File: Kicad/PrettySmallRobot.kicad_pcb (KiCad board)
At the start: 4 copper layers, 25.6 x 25 mm, 56 parts, among them J1 TYPE-C-31-M-12, J2 MOTORA_1, J3 MOTORA_2, J4 MOTORB_1, J5 MOTORB_2, J6 BATT+, J7 GND, U1 DRV8837, U2 DRV8837, U3 MCP73831-2ACI_MC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

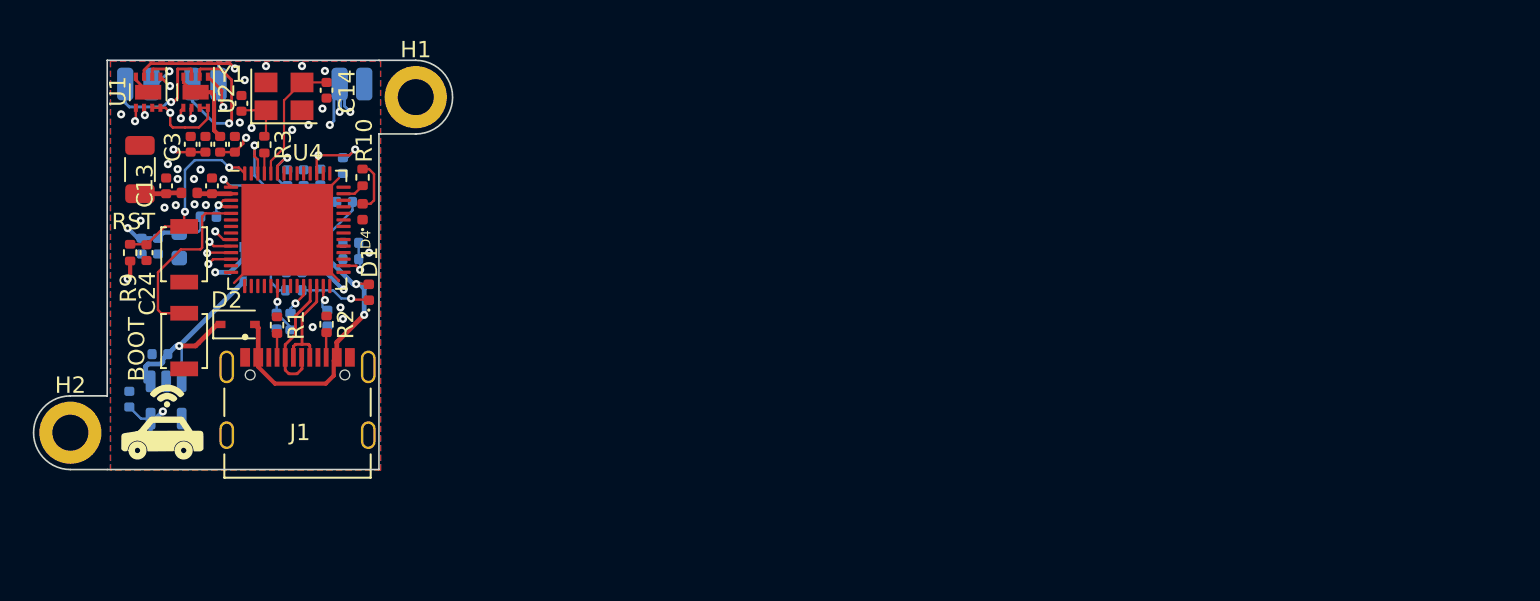
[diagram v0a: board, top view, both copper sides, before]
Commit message: ripped up all routing to start again to fit the new cad
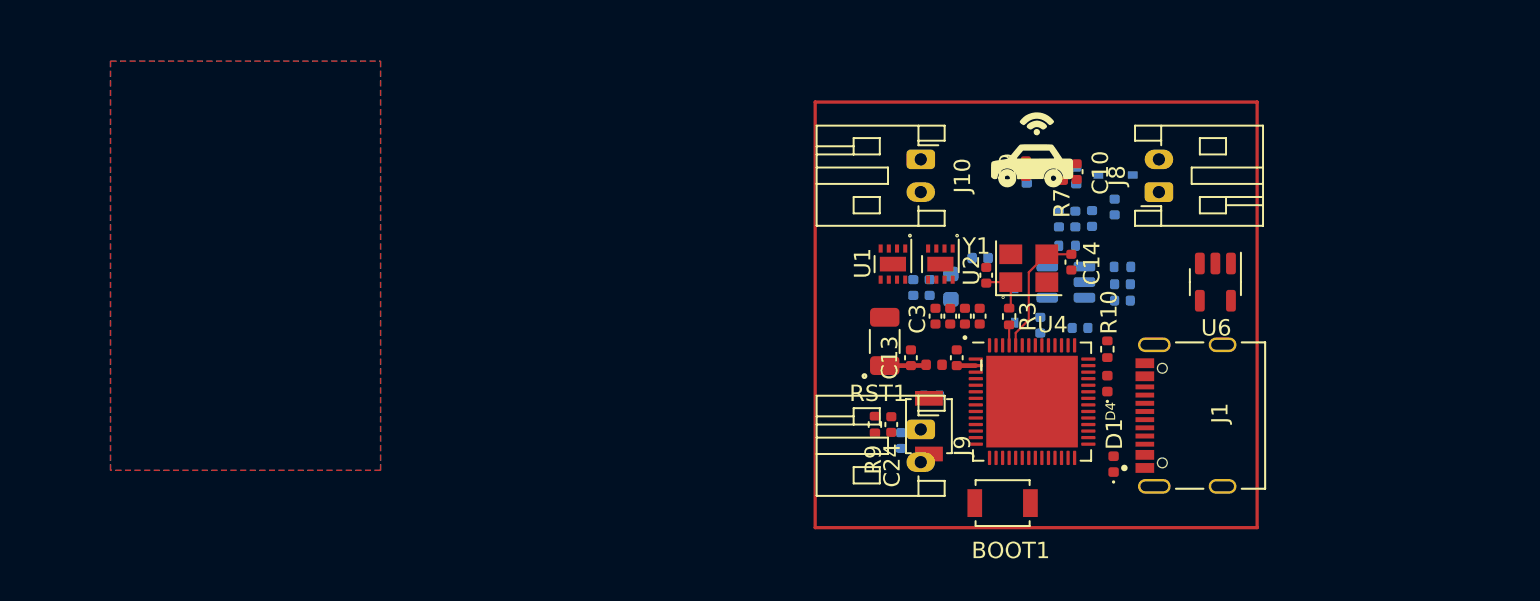
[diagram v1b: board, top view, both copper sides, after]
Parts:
- removed H1, H2: MountingHole, MountingHole:MountingHole_2.2mm_M2_DIN965_Pad
- removed J2: MOTORA_1, Connector_Wire:SolderWirePad_1x01_SMD_1x2mm
- removed J3: MOTORA_2, Connector_Wire:SolderWirePad_1x01_SMD_1x2mm
- removed J4: MOTORB_1, Connector_Wire:SolderWirePad_1x01_SMD_1x2mm
- removed J5: MOTORB_2, Connector_Wire:SolderWirePad_1x01_SMD_1x2mm
- removed J6: BATT+, Connector_Wire:SolderWirePad_1x01_SMD_1x2mm
- removed J7: GND, Connector_Wire:SolderWirePad_1x01_SMD_1x2mm
- added J10: Conn_01x02, Connector_JST:JST_PH_S2B-PH-K_1x02_P2.00mm_Horizontal, F.Cu at (177.0, 102.5)
- added J8: Conn_01x02, Connector_JST:JST_PH_S2B-PH-K_1x02_P2.00mm_Horizontal, F.Cu at (191.6, 104.5)
- added J9: Conn_01x02, Connector_JST:JST_PH_S2B-PH-K_1x02_P2.00mm_Horizontal, F.Cu at (177.0, 119.0)
- C10, C9, R7, U6: moved to F.Cu
- D2, R1, R2: moved to B.Cu
- U3: value MCP73831-2ACI_MC -> MCP73831-2-OT; footprint kicad_footprints:SON50P200X300X100-9N -> Package_TO_SOT_SMD:SOT-23-5
- moved U6 64.5 mm to (195.0, 110.0)
- moved J1 56.5 mm to (195.4, 118.2), turned to 90 degrees
- moved D2 54.4 mm to (188.9, 103.5), turned to 180 degrees
- moved BOOT1 51.0 mm to (182.0, 123.5), turned to 0 degrees
- moved R5 50.6 mm to (189.3, 109.1)
- moved C10 49.7 mm to (186.5, 103.3)
- moved R1 49.7 mm to (186.5, 103.5)
- moved R7 48.0 mm to (185.7, 103.3)
- moved C1 47.2 mm to (178.8, 110.3)
- moved C19 47.2 mm to (187.5, 106.1)
- moved C8 47.2 mm to (188.8, 105.4)
- moved D3 47.2 mm to (182.7, 111.4)
- moved C11 47.2 mm to (189.3, 111.1)
- moved C16 47.2 mm to (189.3, 110.1)
- moved C18 47.2 mm to (186.4, 106.2)
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- renumbered BOOT to BOOT1, RST to RST1
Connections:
- U3 pad 1: /VBUS -> Net-(R5-Pad2)
- U3 pad 2: /VBUS -> GND
- U3 pad 4: +BATT -> /VBUS
- U3 pad 5: Net-(R5-Pad2) -> Net-(R6-Pad2)
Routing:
- net +BATT: track 64.8 -> 0.00 mm, vias 8 -> 0
- net +3V3: track 35.6 -> 0.00 mm, vias 11 -> 0
- net /VBUS: track 22.9 -> 0.00 mm, vias 2 -> 0
- net GND: track 22.1 -> 0.00 mm, vias 24 -> 0
- net /VDDA: track 16.2 -> 0.00 mm, vias 3 -> 0
- net /MOTORB_IN2: track 16.0 -> 0.00 mm, vias 2 -> 0
- net /MOTORA_IN2: track 15.9 -> 0.00 mm, vias 2 -> 0
- net Net-(C22-Pad1): track 14.5 -> 0.00 mm, vias 1 -> 0
- net /MOTORA_IN1: track 14.2 -> 0.00 mm, vias 2 -> 0
- net /MOTORB_IN1: track 13.5 -> 0.00 mm, vias 2 -> 0
- net /~{RESET}: track 11.5 -> 0.00 mm, vias 2 -> 0
- net /BOOT: track 11.0 -> 0.00 mm
- net /MOTORB_OUT1: track 9.24 -> 0.00 mm, vias 1 -> 0
- net /MOTORA_OUT2: track 8.61 -> 0.00 mm, vias 1 -> 0
- net /MOTORB_OUT2: track 7.75 -> 0.00 mm, vias 1 -> 0
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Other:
- board outline removed
- board text added: "Mounting Clip"

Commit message: resized board to 29x27mm
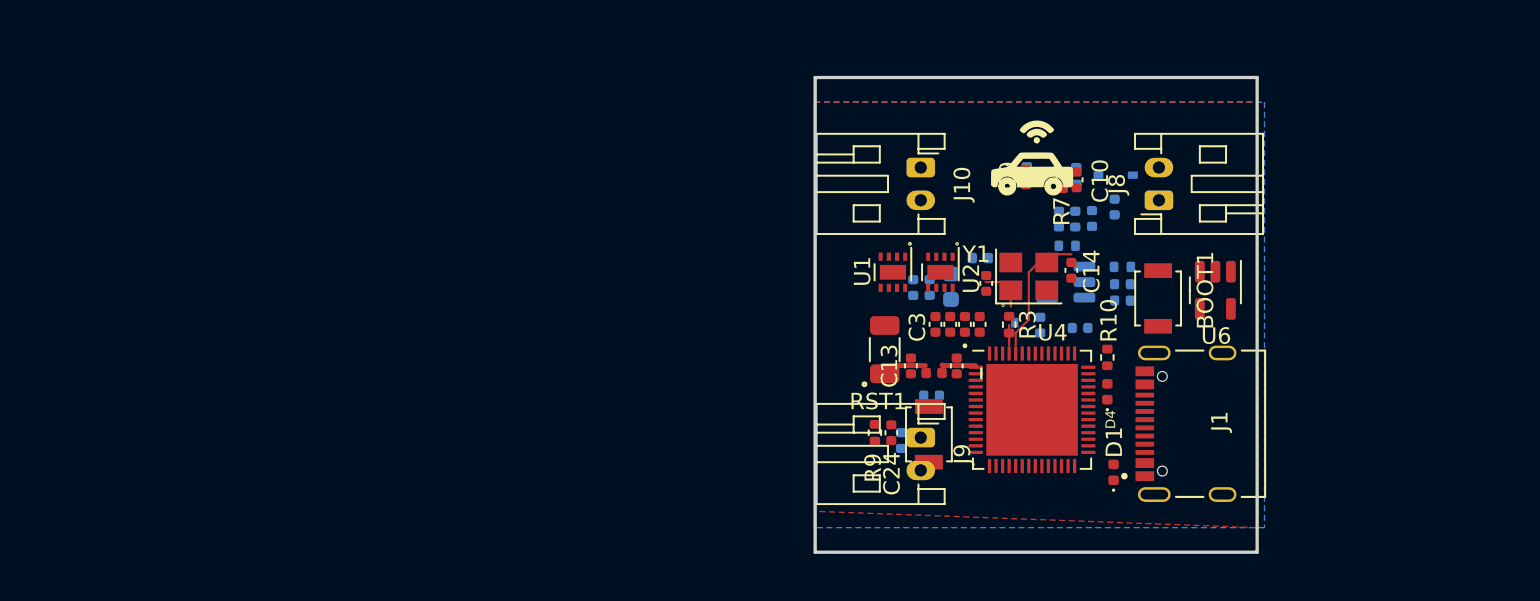
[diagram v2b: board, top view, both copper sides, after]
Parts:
- moved BOOT1 15.7 mm to (191.5, 111.0), turned to 90 degrees
- moved AE1 0.50 mm to (174.8, 114.1)
- moved C10 0.50 mm to (186.5, 103.8)
- moved C13 0.50 mm to (176.4, 115.1)
- moved C14 0.50 mm to (186.2, 109.3)
- moved C15 0.50 mm to (181.0, 110.1)
- moved C17 0.50 mm to (179.2, 115.1)
- moved C2 0.50 mm to (180.6, 112.6)
- moved C24 0.50 mm to (175.2, 119.2)
- moved C3 0.50 mm to (177.9, 112.6)
- moved C6 0.50 mm to (178.8, 112.6)
- moved C7 0.50 mm to (179.7, 112.6)
- moved C9 0.50 mm to (183.4, 103.6)
- moved D1 0.50 mm to (188.8, 121.6)
- moved D4 0.50 mm to (188.4, 116.7)
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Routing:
- net Net-(C17-Pad1): track 1.16 -> 2.08 mm
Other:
- board outline added: 27 x 29 mm

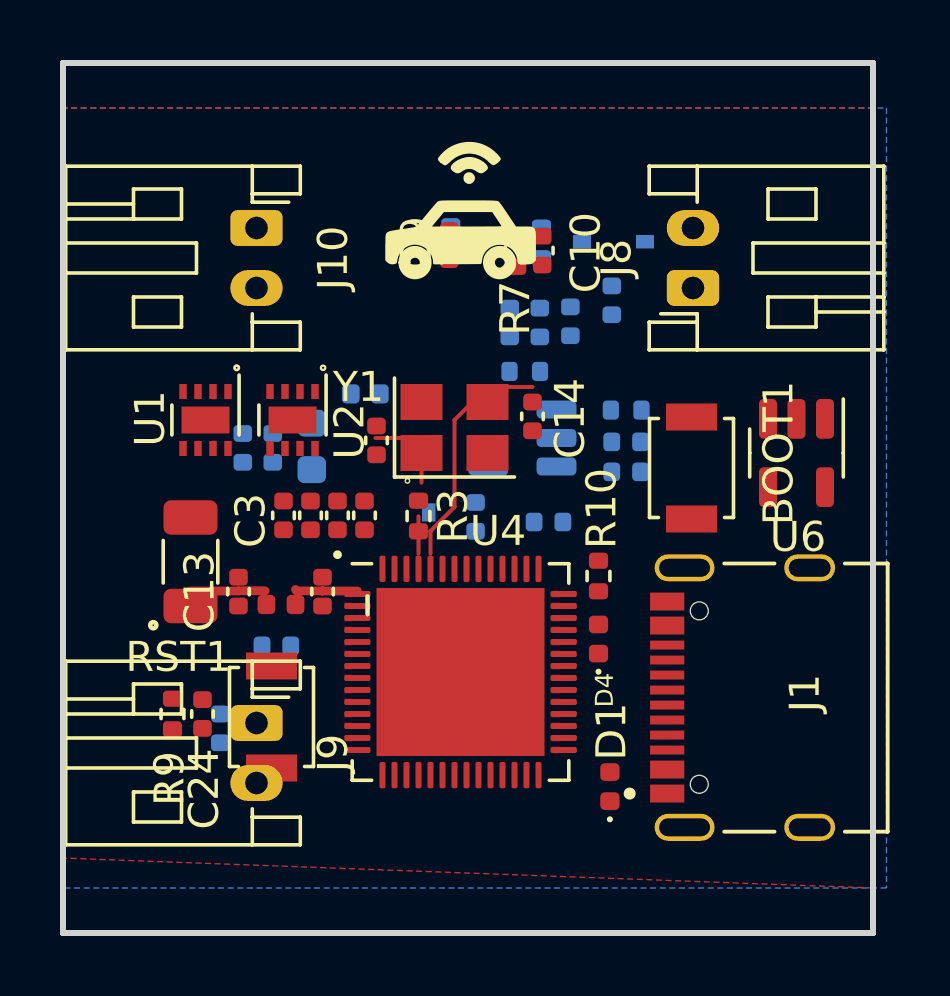
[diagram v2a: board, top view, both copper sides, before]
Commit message: resized board again to 29x26mm
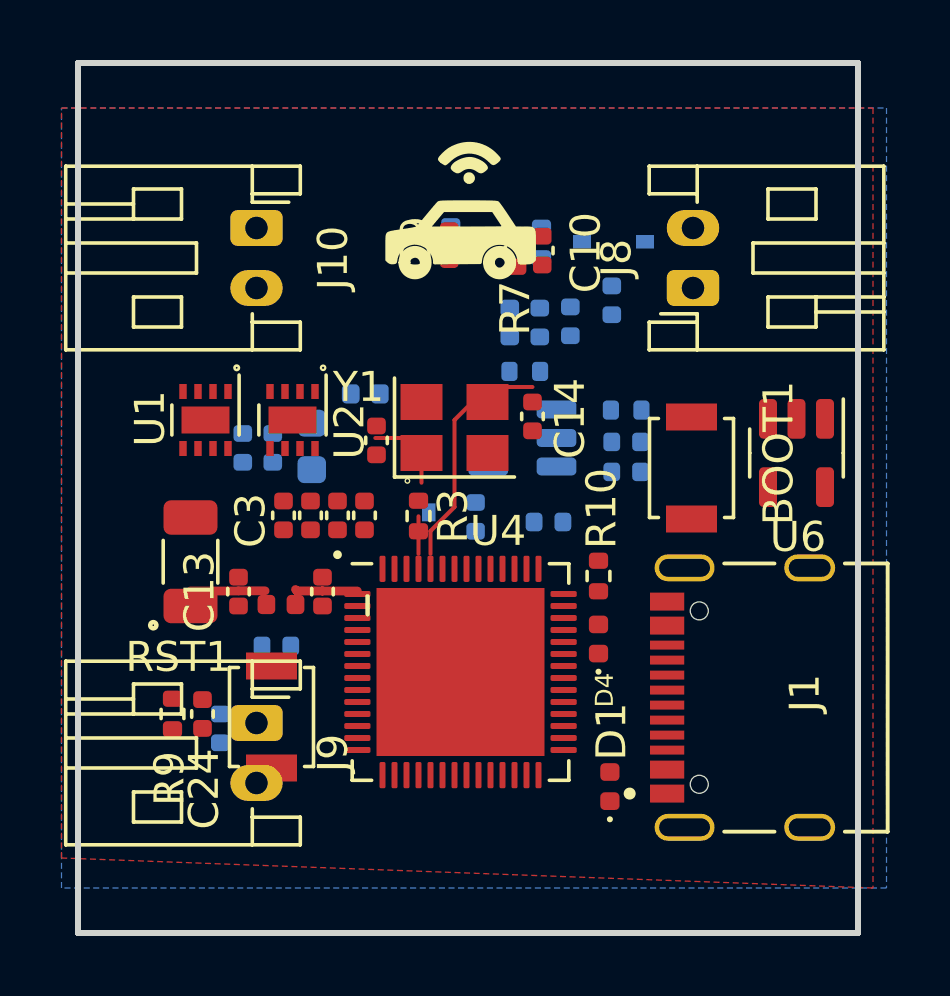
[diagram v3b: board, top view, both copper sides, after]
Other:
- board size 27 x 29 mm -> 26 x 29 mm
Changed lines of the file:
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@@
       (xy 184.129503 100.179194)
     ) (layer "F.SilkS") (width 0.1) (fill solid))
-  (gr_rect (start 170.55 97.5) (end 197.55 126.5) (layer "Edge.Cuts") (width 0.2) (fill none))
+  (gr_rect (start 171.05 97.5) (end 197.05 126.5) (layer "Edge.Cuts") (width 0.2) (fill none))
   (gr_circle (center 176.5 107.65) (end 176.6 107.65) (layer "F.Fab") (width 0.1) (fill none))
   (gr_text "Mounting Clip" (at 183.55 127) (layer "Cmts.User")

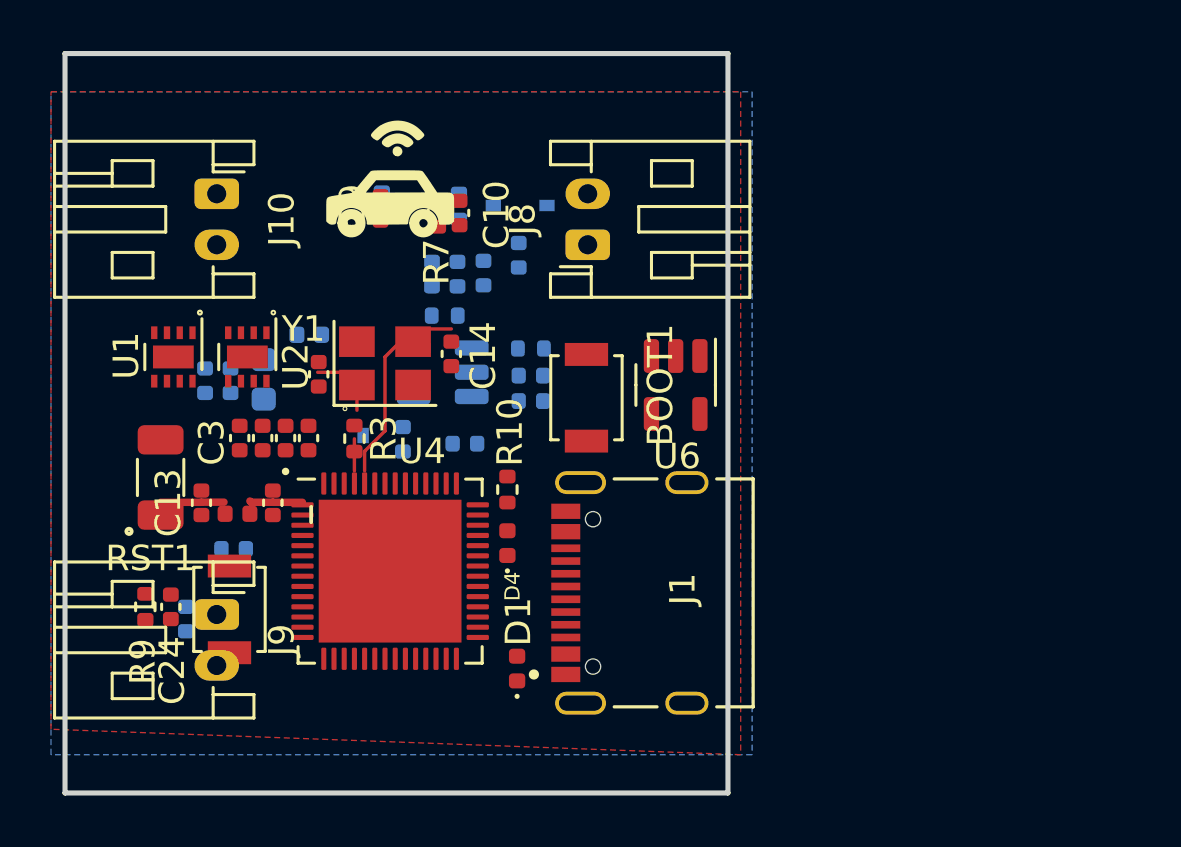
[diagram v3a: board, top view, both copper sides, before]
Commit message: re added jst connectors, removed mount holes
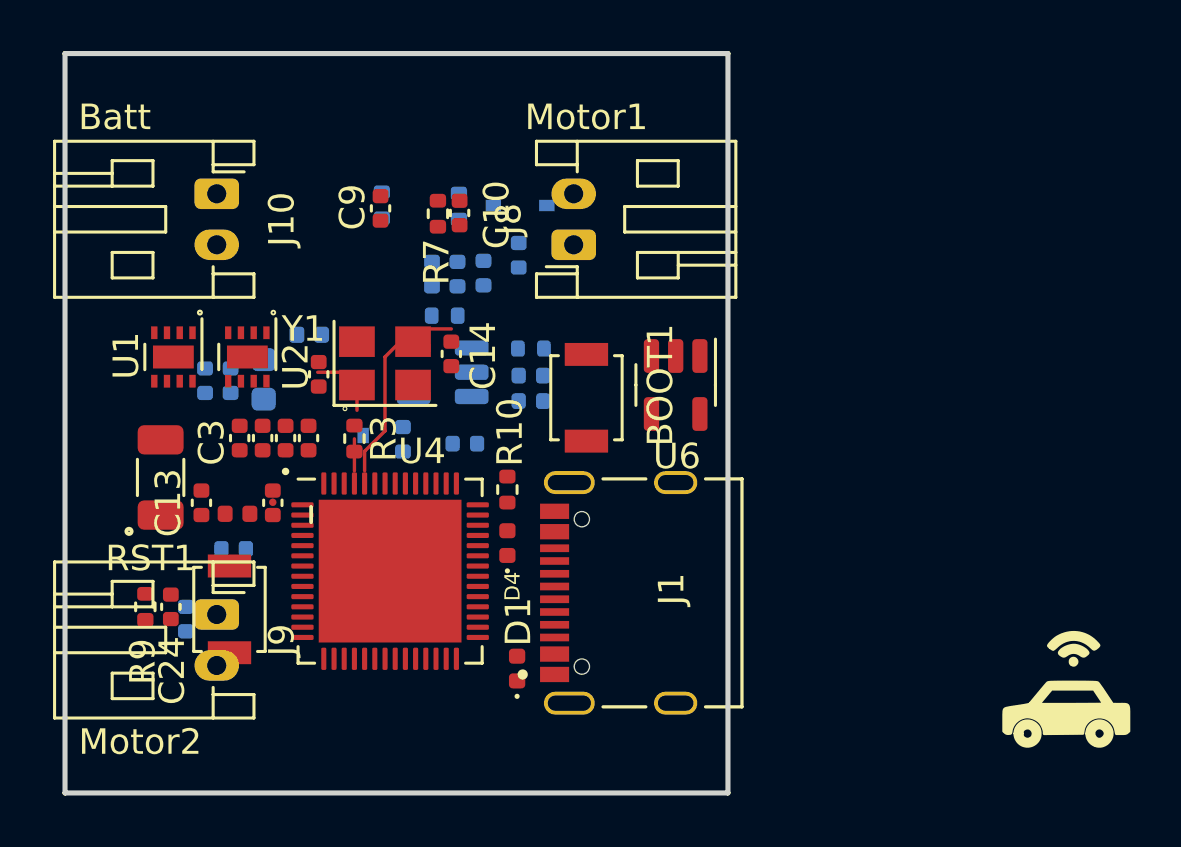
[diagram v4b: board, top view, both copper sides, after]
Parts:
- moved J8 0.55 mm to (191.0, 105.0)
- moved J1 0.44 mm to (195.0, 118.7)
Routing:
- net Net-(AE1-Pad1): track 2.48 -> 0.00 mm
- net Net-(C17-Pad1): track 2.08 -> 0.00 mm
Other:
- board text added: "Batt"
- board text added: "Motor1"
- board text added: "Motor2"
